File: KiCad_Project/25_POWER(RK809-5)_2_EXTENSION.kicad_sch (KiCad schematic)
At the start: 15 parts

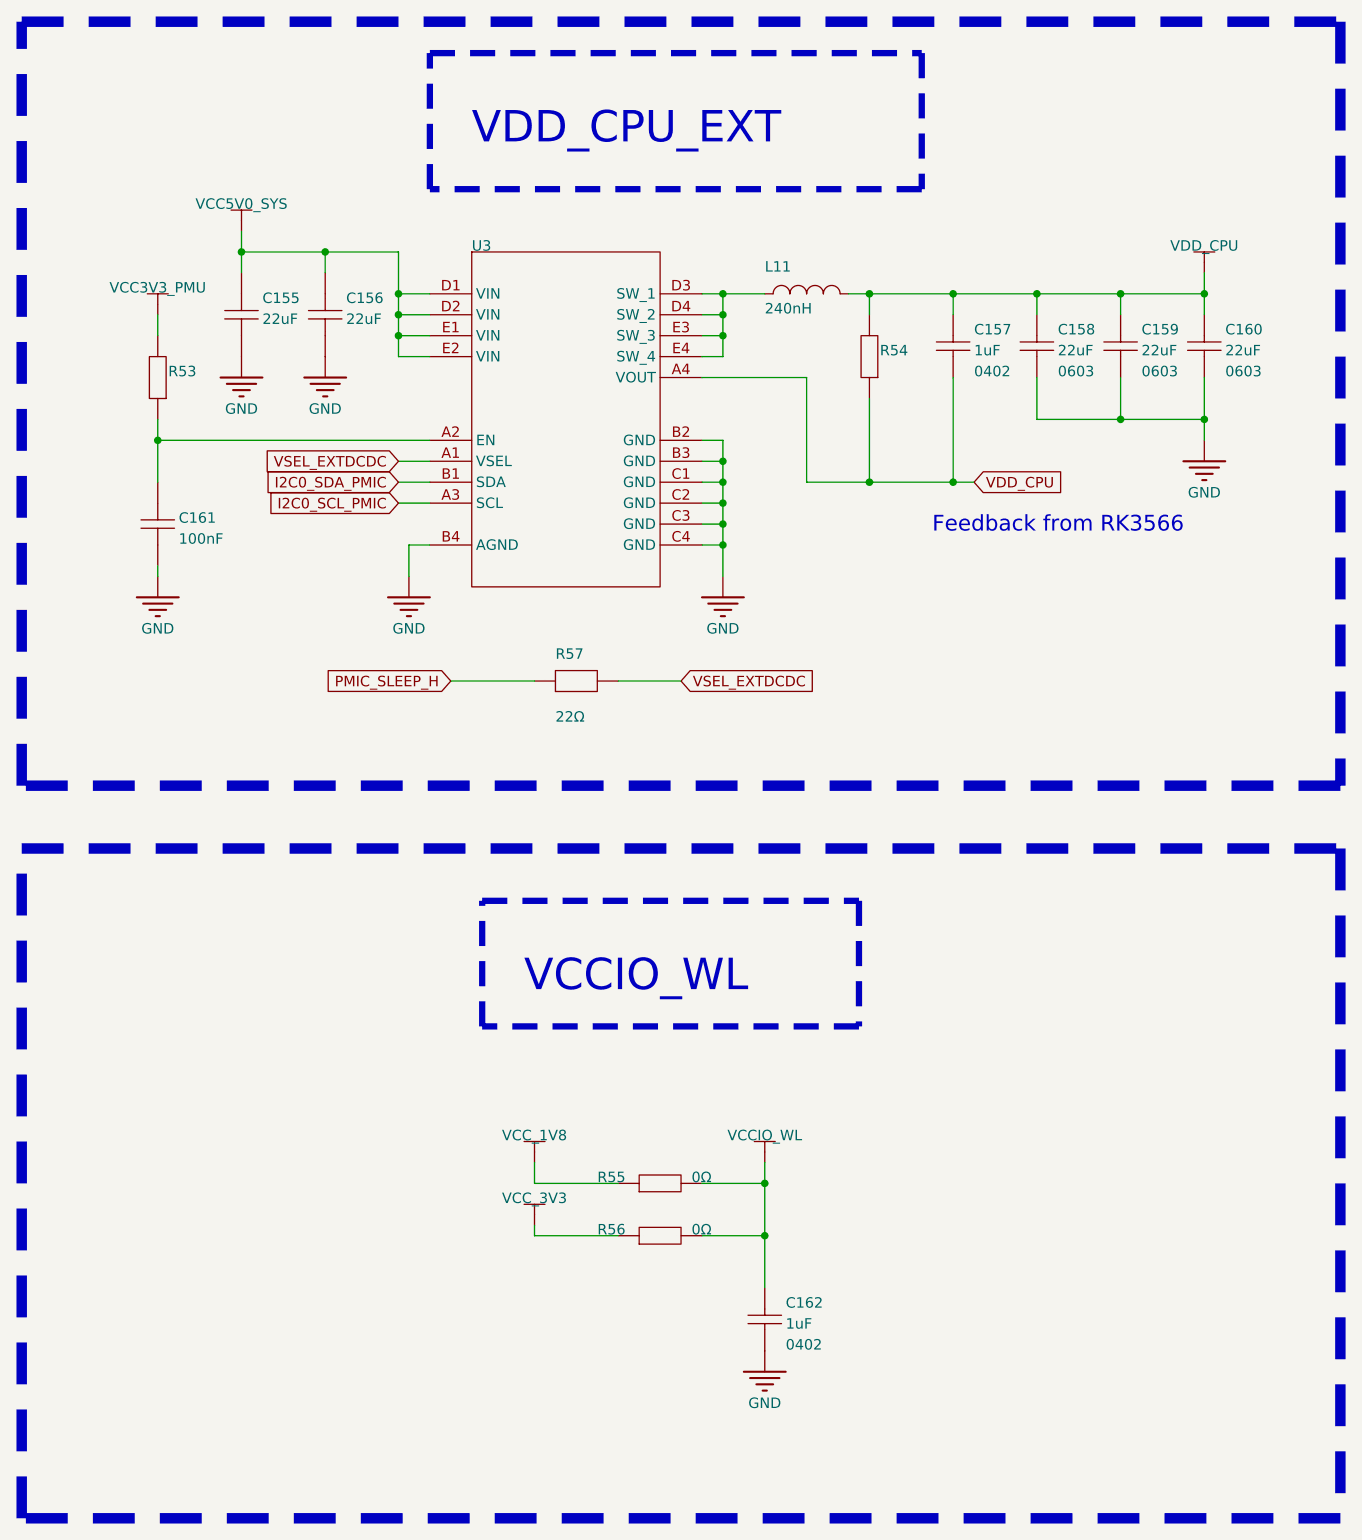
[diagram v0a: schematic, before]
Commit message: Update additional PCBs
Add WIFI PCB to get best antenna
Add Display Debbugger to get interface pinout
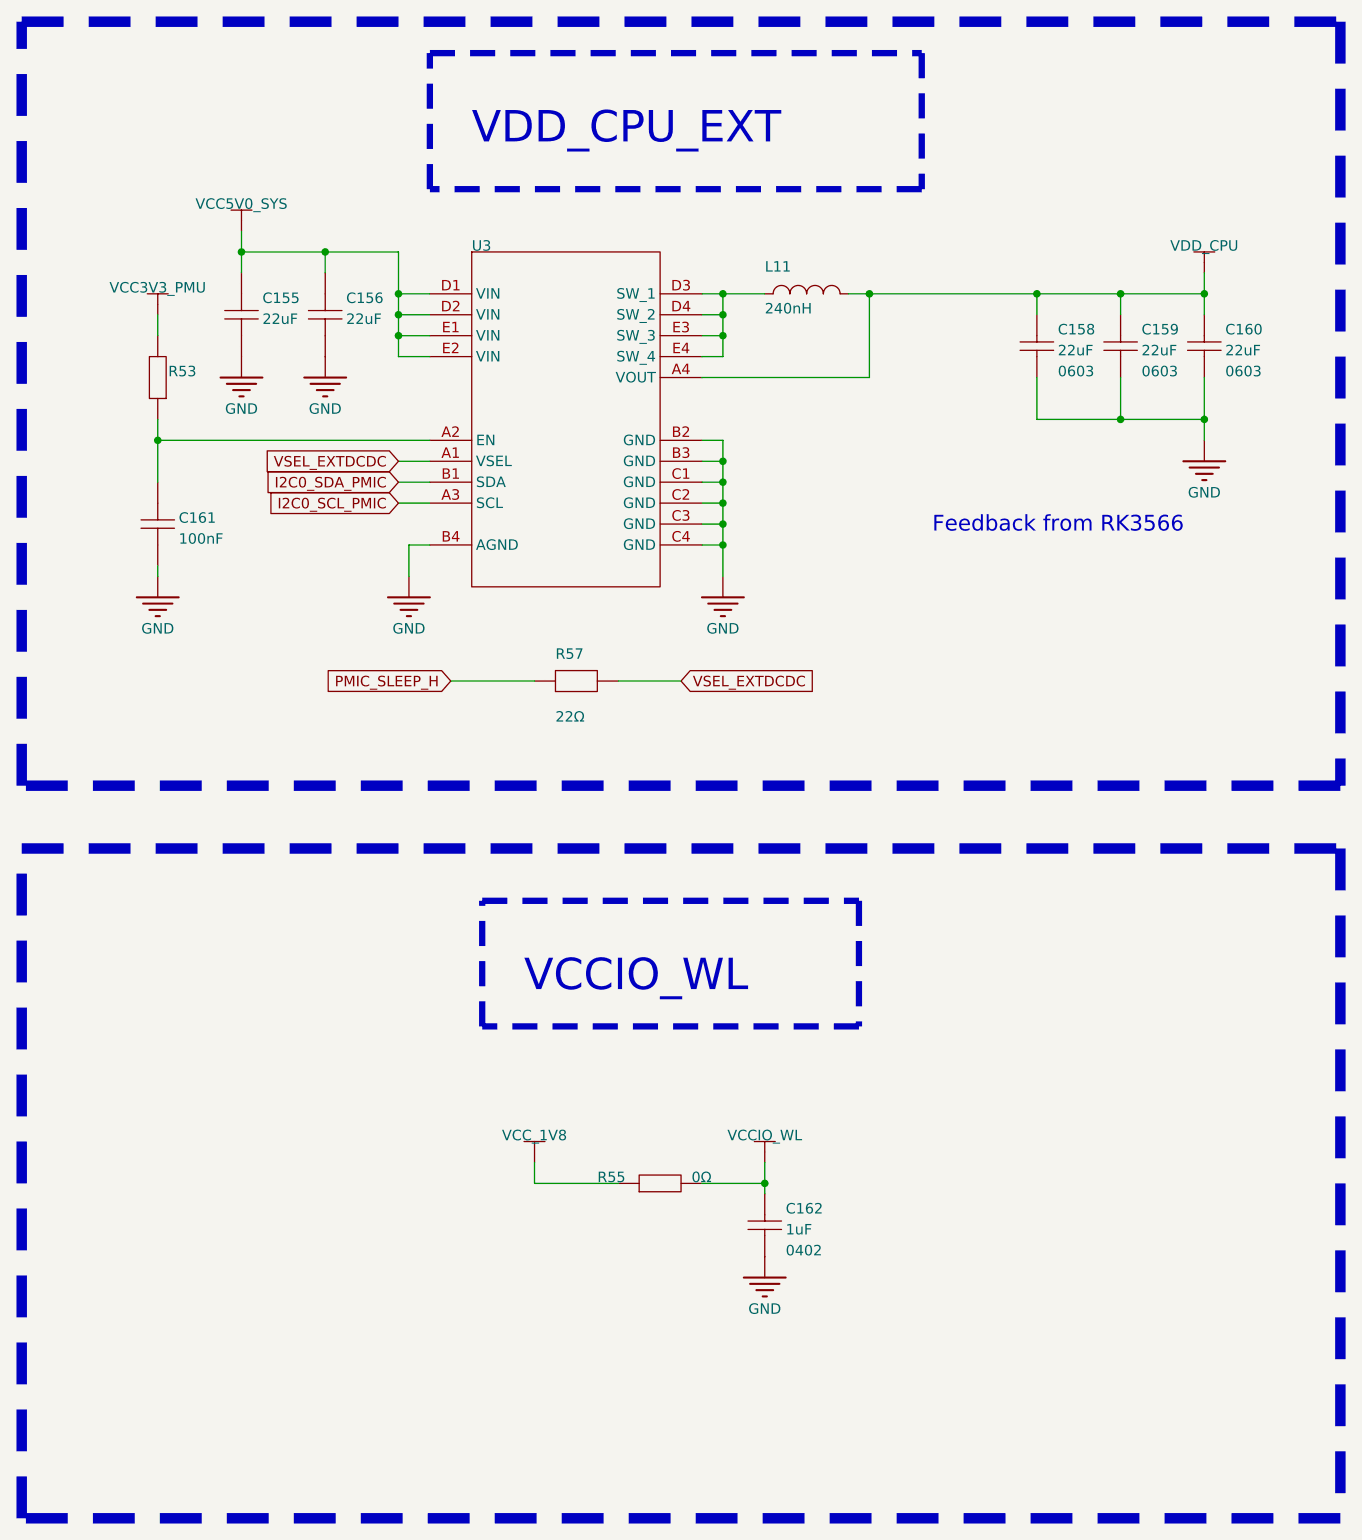
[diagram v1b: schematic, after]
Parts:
- removed C157: 1uF, Capacitor_SMD:C_0402_1005Metric, symbol LCSC Taish-easyedapro:CL05A105KP5NNNC
- removed R54: 0402WGF1000TCE, LCSC Taish-easyedapro:R0402, symbol LCSC Taish-easyedapro:0402WGF1000TCE
- removed R56: 0Ω, LCSC Taish-easyedapro:R0402, symbol LCSC Taish-easyedapro:ERJ2GE0R00X
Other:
- moved on the sheet: C162
